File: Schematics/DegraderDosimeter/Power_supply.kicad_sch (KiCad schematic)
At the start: 25 parts, among them U4 LM60430DRPKR, U6 TC1262-33, U7 TC1262-33

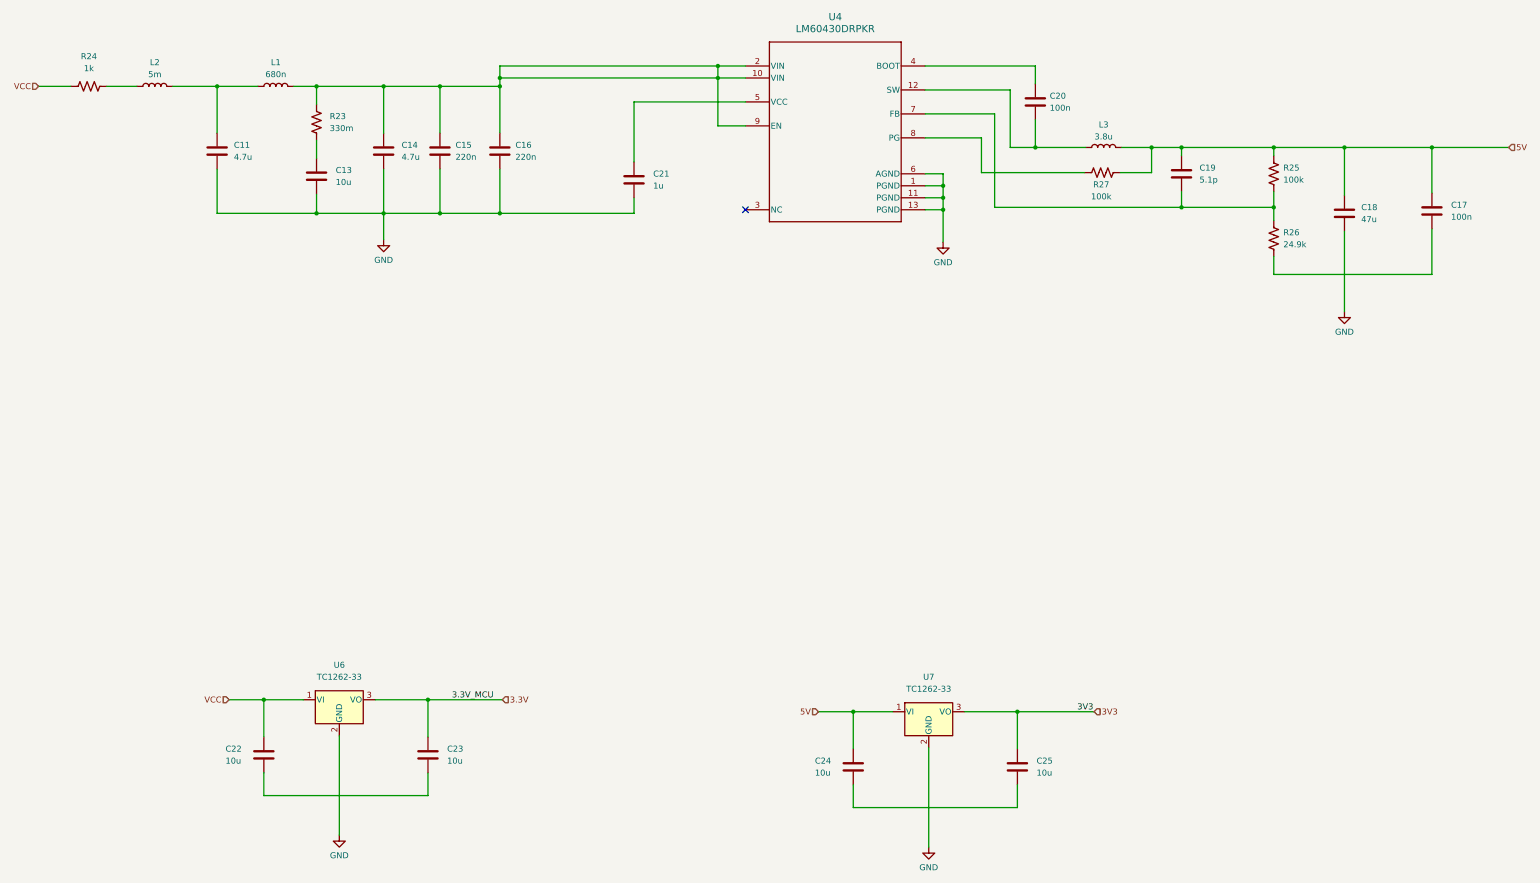
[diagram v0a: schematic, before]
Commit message: Use 1206 for every resistor in the project
The Ethernet sheet was the only one on 0402, set that way to match the
MB1364 BOM. The other four sheets already used
Resistor_SMD:R_1206_3216Metric_Pad1.30x1.75mm_HandSolder, so move the
20 Ethernet resistors to the same footprint. All 37 resistors in the
project now share one package, which suits hand assembly.

This deviates from the ST reference for the eight resistors on the
high-speed nets: R3-R6 (33R RMII series) and R12-R15 (49R9 centre-tap
terminations). 1206 has more parasitic inductance and larger pads than
the 0402 parts ST fits. 100BASE-TX is tolerant enough that this should
still work, but 0402 would be the better choice on those eight.

This commit also captures schematic edits made in KiCad outside this
session: a project-wide re-annotation and the removal of R21/R22, the
two 75R resistors that terminated the jack's unused pairs.

Co-Authored-By: Claude Opus 5 <noreply@anthropic.com>
Claude-Session: https://claude.ai/code/session_01Ej9hevrS5JU2uwVi6UHQUS
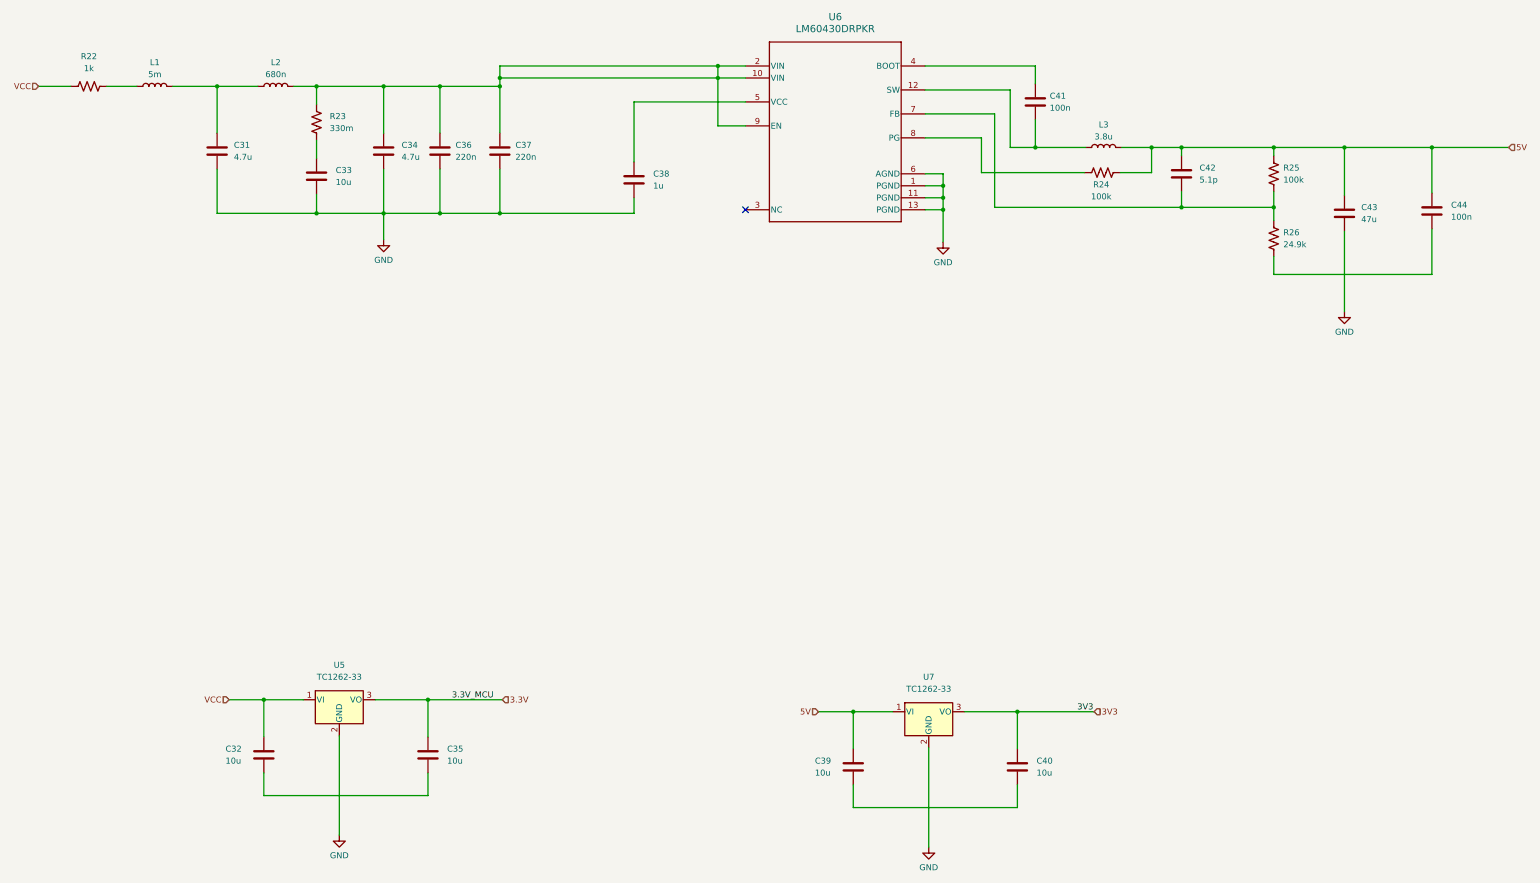
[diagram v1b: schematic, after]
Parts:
- U6: renamed from U4; footprint RPK0013A-MFG -> RPK0013A-MFG:RPK0013A-MFG
- renumbered C11 to C31, C22 to C32, C13 to C33, C14 to C34, C23 to C35, C15 to C36, C16 to C37, C21 to C38, C24 to C39, C25 to C40, C20 to C41, C19 to C42, C18 to C43, C17 to C44, L2 to L1, L1 to L2, R24 to R22, R27 to R24, U6 to U5
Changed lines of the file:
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@@
 		(dnp no)
 		(fields_autoplaced yes)
-		(property "Reference" "#PWR016"
+		(property "Reference" "#PWR040"
 			(at 132.08 97.282 0)
 			(hide yes)
@@
 			(project "DegraderDosimeter"
 				(path "/f3c83d46-b432-4960-ae55-27eb620ca6d0/ad3f19ac-af46-441e-8be8-2329fde7a5e2"
-					(reference "#PWR016")
+					(reference "#PWR040")
 					(unit 1)
 				)
@@
 		(dnp no)
 		(fields_autoplaced yes)
-		(property "Reference" "#PWR018"
+		(property "Reference" "#PWR043"
 			(at 335.788 112.522 0)
 			(hide yes)
@@
 			(project "DegraderDosimeter"
 				(path "/f3c83d46-b432-4960-ae55-27eb620ca6d0/ad3f19ac-af46-441e-8be8-2329fde7a5e2"
-					(reference "#PWR018")
+					(reference "#PWR043")
 					(unit 1)
 				)
@@
 		(dnp no)
 		(fields_autoplaced yes)
-		(property "Reference" "R24"
+		(property "Reference" "R22"
 			(at 69.596 52.07 90)
 			(show_name no)
@@
 			(project "DegraderDosimeter"
 				(path "/f3c83d46-b432-4960-ae55-27eb620ca6d0/ad3f19ac-af46-441e-8be8-2329fde7a5e2"
-					(reference "R24")
+					(reference "R22")
 					(unit 1)
 				)
@@
 		(dnp no)
 		(fields_autoplaced yes)
-		(property "Reference" "C23"
+		(property "Reference" "C35"
 			(at 145.542 198.8819 0)
 			(show_name no)
@@
 			(project "DegraderDosimeter"
 				(path "/f3c83d46-b432-4960-ae55-27eb620ca6d0/ad3f19ac-af46-441e-8be8-2329fde7a5e2"
-					(reference "C23")
+					(reference "C35")
 					(unit 1)
 				)
@@
 		(dnp no)
 		(fields_autoplaced yes)
-		(property "Reference" "C13"
+		(property "Reference" "C33"
 			(at 121.92 76.1999 0)
 			(show_name no)
@@
 			(project "DegraderDosimeter"
 				(path "/f3c83d46-b432-4960-ae55-27eb620ca6d0/ad3f19ac-af46-441e-8be8-2329fde7a5e2"
-					(reference "C13")
+					(reference "C33")
 					(unit 1)
 				)
@@
 		(dnp no)
 		(fields_autoplaced yes)
-		(property "Reference" "#PWR020"
+		(property "Reference" "#PWR039"
 			(at 122.682 223.52 0)
 			(hide yes)
@@
 			(project "DegraderDosimeter"
 				(path "/f3c83d46-b432-4960-ae55-27eb620ca6d0/ad3f19ac-af46-441e-8be8-2329fde7a5e2"
-					(reference "#PWR020")
+					(reference "#PWR039")
 					(unit 1)
 				)
@@
 		(dnp no)
 		(fields_autoplaced yes)
-		(property "Reference" "L2"
+		(property "Reference" "L1"
 			(at 83.566 53.34 90)
 			(show_name no)
@@
 			(project "DegraderDosimeter"
 				(path "/f3c83d46-b432-4960-ae55-27eb620ca6d0/ad3f19ac-af46-441e-8be8-2329fde7a5e2"
-					(reference "L2")
+					(reference "L1")
 					(unit 1)
 				)
@@
 		(in_pos_files yes)
 		(dnp no)
-		(property "Reference" "C22"
+		(property "Reference" "C32"
 			(at 98.552 198.882 0)
 			(show_name no)
@@
 			(project "DegraderDosimeter"
 				(path "/f3c83d46-b432-4960-ae55-27eb620ca6d0/ad3f19ac-af46-441e-8be8-2329fde7a5e2"
-					(reference "C22")
+					(reference "C32")
 					(unit 1)
 				)
@@
 		(dnp no)
 		(fields_autoplaced yes)
-		(property "Reference" "#PWR019"
+		(property "Reference" "#PWR042"
 			(at 250.698 97.79 0)
 			(hide yes)
@@
 			(project "DegraderDosimeter"
 				(path "/f3c83d46-b432-4960-ae55-27eb620ca6d0/ad3f19ac-af46-441e-8be8-2329fde7a5e2"
-					(reference "#PWR019")
+					(reference "#PWR042")
 					(unit 1)
 				)
@@
 		(in_pos_files yes)
 		(dnp no)
-		(property "Reference" "C24"
+		(property "Reference" "C39"
 			(at 223.52 201.422 0)
 			(show_name no)
@@
 			(project "DegraderDosimeter"
 				(path "/f3c83d46-b432-4960-ae55-27eb620ca6d0/ad3f19ac-af46-441e-8be8-2329fde7a5e2"
-					(reference "C24")
+					(reference "C39")
 					(unit 1)
 				)
@@
 		(dnp no)
 		(fields_autoplaced yes)
-		(property "Reference" "C20"
+		(property "Reference" "C41"
 			(at 273.304 60.4519 0)
 			(show_name no)
@@
 			(project "DegraderDosimeter"
 				(path "/f3c83d46-b432-4960-ae55-27eb620ca6d0/ad3f19ac-af46-441e-8be8-2329fde7a5e2"
-					(reference "C20")
+					(reference "C41")
 					(unit 1)
 				)
@@
 		(dnp no)
 		(fields_autoplaced yes)
-		(property "Reference" "C14"
+		(property "Reference" "C34"
 			(at 135.89 70.8659 0)
 			(show_name no)
@@
 			(project "DegraderDosimeter"
 				(path "/f3c83d46-b432-4960-ae55-27eb620ca6d0/ad3f19ac-af46-441e-8be8-2329fde7a5e2"
-					(reference "C14")
+					(reference "C34")
 					(unit 1)
 				)
@@
 		(dnp no)
 		(fields_autoplaced yes)
-		(property "Reference" "C18"
+		(property "Reference" "C43"
 			(at 339.344 84.0739 0)
 			(show_name no)
@@
 			(project "DegraderDosimeter"
 				(path "/f3c83d46-b432-4960-ae55-27eb620ca6d0/ad3f19ac-af46-441e-8be8-2329fde7a5e2"
-					(reference "C18")
+					(reference "C43")
 					(unit 1)
 				)
@@
 		(dnp no)
 		(fields_autoplaced yes)
-		(property "Reference" "#PWR021"
+		(property "Reference" "#PWR041"
 			(at 247.65 226.06 0)
 			(hide yes)
@@
 			(project "DegraderDosimeter"
 				(path "/f3c83d46-b432-4960-ae55-27eb620ca6d0/ad3f19ac-af46-441e-8be8-2329fde7a5e2"
-					(reference "#PWR021")
+					(reference "#PWR041")
 					(unit 1)
 				)
@@
 		(dnp no)
 		(fields_autoplaced yes)
-		(property "Reference" "C15"
+		(property "Reference" "C36"
 			(at 147.32 70.8659 0)
 			(show_name no)
@@
 			(project "DegraderDosimeter"
 				(path "/f3c83d46-b432-4960-ae55-27eb620ca6d0/ad3f19ac-af46-441e-8be8-2329fde7a5e2"
-					(reference "C15")
+					(reference "C36")
 					(unit 1)
 				)
@@
 		(dnp no)
 		(fields_autoplaced yes)
-		(property "Reference" "C25"
+		(property "Reference" "C40"
 			(at 270.51 201.4219 0)
 			(show_name no)
@@
 			(project "DegraderDosimeter"
 				(path "/f3c83d46-b432-4960-ae55-27eb620ca6d0/ad3f19ac-af46-441e-8be8-2329fde7a5e2"
-					(reference "C25")
+					(reference "C40")
 					(unit 1)
 				)
@@
 		(dnp no)
 		(fields_autoplaced yes)
-		(property "Reference" "U4"
+		(property "Reference" "U6"
 			(at 227.838 43.688 0)
 			(show_name no)
@@
 			)
 		)
-		(property "Footprint" "RPK0013A-MFG"
+		(property "Footprint" "RPK0013A-MFG:RPK0013A-MFG"
 			(at 213.868 54.102 0)
 			(hide yes)
@@
 			(project "DegraderDosimeter"
 				(path "/f3c83d46-b432-4960-ae55-27eb620ca6d0/ad3f19ac-af46-441e-8be8-2329fde7a5e2"
-					(reference "U4")
+					(reference "U6")
 					(unit 1)
 				)
@@
 		(dnp no)
 		(fields_autoplaced yes)
-		(property "Reference" "L1"
+		(property "Reference" "L2"
 			(at 109.22 53.34 90)
 			(show_name no)
@@
 			(project "DegraderDosimeter"
 				(path "/f3c83d46-b432-4960-ae55-27eb620ca6d0/ad3f19ac-af46-441e-8be8-2329fde7a5e2"
-					(reference "L1")
+					(reference "L2")
 					(unit 1)
 				)
@@
 		(dnp no)
 		(fields_autoplaced yes)
-		(property "Reference" "C16"
+		(property "Reference" "C37"
 			(at 160.02 70.8659 0)
 			(show_name no)
@@
 			(project "DegraderDosimeter"
 				(path "/f3c83d46-b432-4960-ae55-27eb620ca6d0/ad3f19ac-af46-441e-8be8-2329fde7a5e2"
-					(reference "C16")
+					(reference "C37")
 					(unit 1)
 				)
@@
 		(dnp no)
 		(fields_autoplaced yes)
-		(property "Reference" "C19"
+		(property "Reference" "C42"
 			(at 305.054 75.6919 0)
 			(show_name no)
@@
 			(project "DegraderDosimeter"
 				(path "/f3c83d46-b432-4960-ae55-27eb620ca6d0/ad3f19ac-af46-441e-8be8-2329fde7a5e2"
-					(reference "C19")
+					(reference "C42")
 					(unit 1)
 				)
@@
 		(dnp no)
 		(fields_autoplaced yes)
-		(property "Reference" "C17"
+		(property "Reference" "C44"
 			(at 358.394 83.5659 0)
 			(show_name no)
@@
 			(project "DegraderDosimeter"
 				(path "/f3c83d46-b432-4960-ae55-27eb620ca6d0/ad3f19ac-af46-441e-8be8-2329fde7a5e2"
-					(reference "C17")
+					(reference "C44")
 					(unit 1)
 				)
@@
 		(dnp no)
 		(fields_autoplaced yes)
-		(property "Reference" "C11"
+		(property "Reference" "C31"
 			(at 100.33 70.8659 0)
 			(show_name no)
@@
 			(project "DegraderDosimeter"
 				(path "/f3c83d46-b432-4960-ae55-27eb620ca6d0/ad3f19ac-af46-441e-8be8-2329fde7a5e2"
-					(reference "C11")
+					(reference "C31")
 					(unit 1)
 				)
@@
 		(dnp no)
 		(fields_autoplaced yes)
-		(property "Reference" "U6"
+		(property "Reference" "U5"
 			(at 122.682 181.102 0)
 			(show_name no)
@@
 			(project "DegraderDosimeter"
 				(path "/f3c83d46-b432-4960-ae55-27eb620ca6d0/ad3f19ac-af46-441e-8be8-2329fde7a5e2"
-					(reference "U6")
+					(reference "U5")
 					(unit 1)
 				)
@@
 		(dnp no)
 		(fields_autoplaced yes)
-		(property "Reference" "C21"
+		(property "Reference" "C38"
 			(at 189.23 76.9619 0)
 			(show_name no)
@@
 			(project "DegraderDosimeter"
 				(path "/f3c83d46-b432-4960-ae55-27eb620ca6d0/ad3f19ac-af46-441e-8be8-2329fde7a5e2"
-					(reference "C21")
+					(reference "C38")
 					(unit 1)
 				)
@@
 		(in_pos_files yes)
 		(dnp no)
-		(property "Reference" "R27"
+		(property "Reference" "R24"
 			(at 284.226 79.248 90)
 			(show_name no)
@@
 			(project "DegraderDosimeter"
 				(path "/f3c83d46-b432-4960-ae55-27eb620ca6d0/ad3f19ac-af46-441e-8be8-2329fde7a5e2"
-					(reference "R27")
-					(unit 1)
-				)
+					(reference "R24")
+					(unit 1)
+				)
